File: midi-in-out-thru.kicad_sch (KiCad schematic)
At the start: 20 parts, among them CN1 uC, M1 IN, M2 OUT, M3 THRU, U1 6N138, U1 74HC14, U101 74HC14

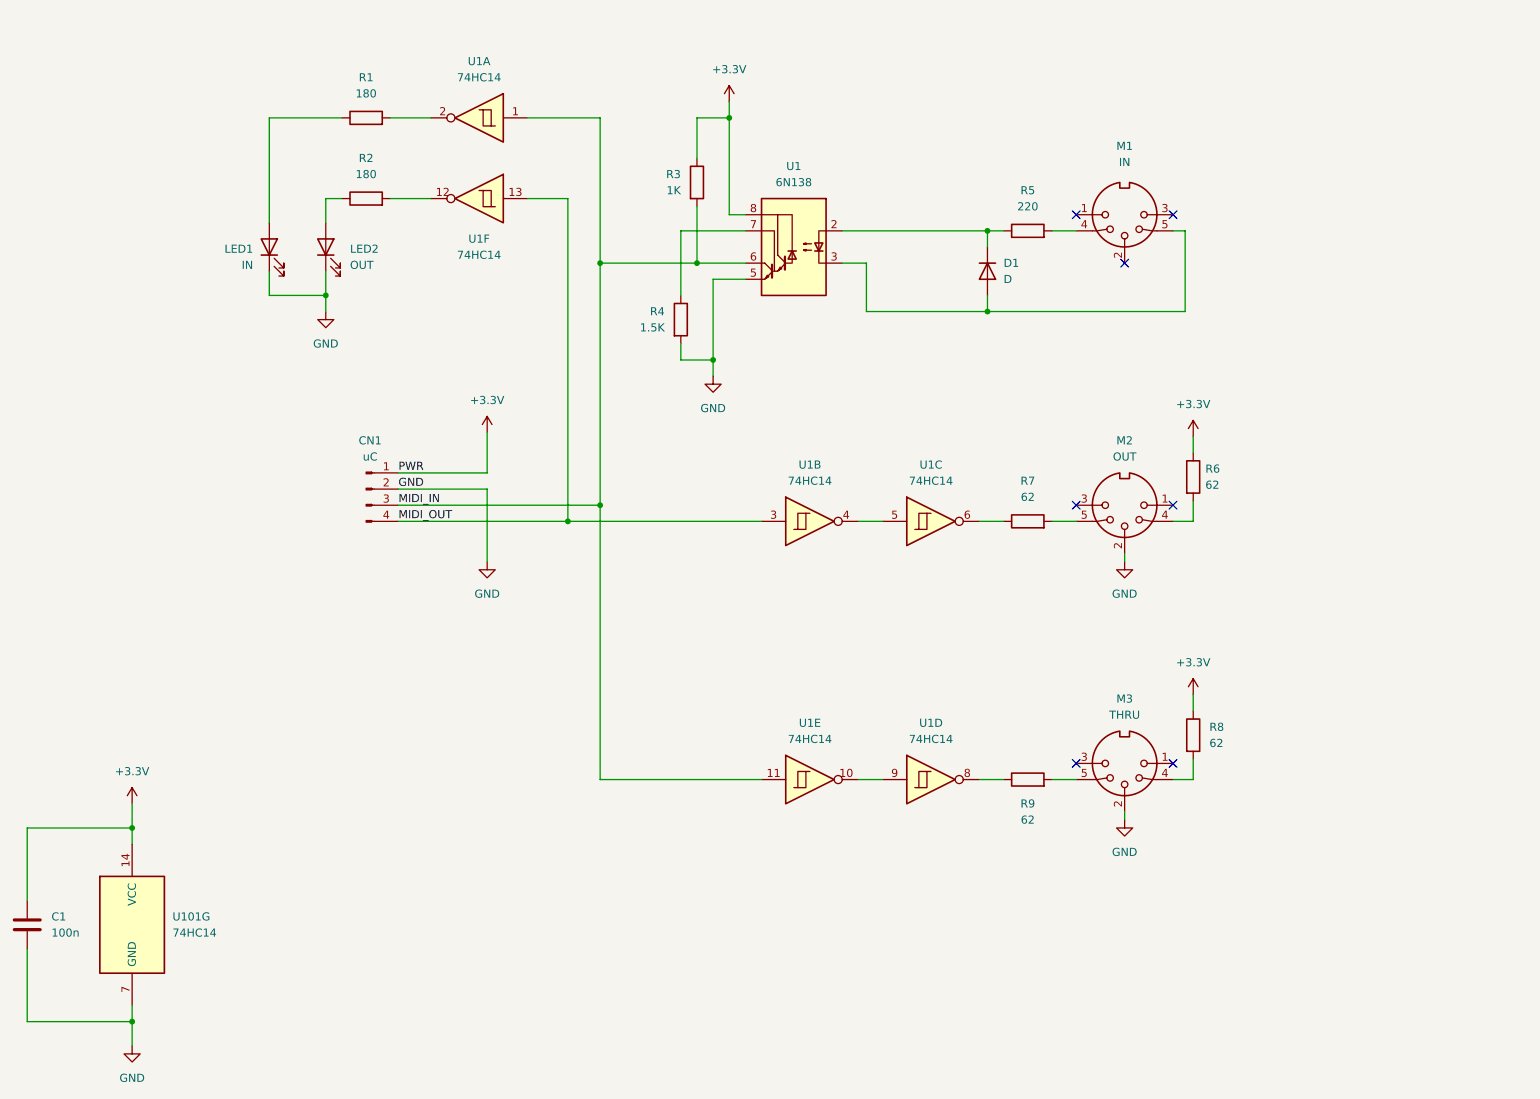
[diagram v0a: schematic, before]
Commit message: Use H11L1
Resistor values taken from CA-033 Update 2014
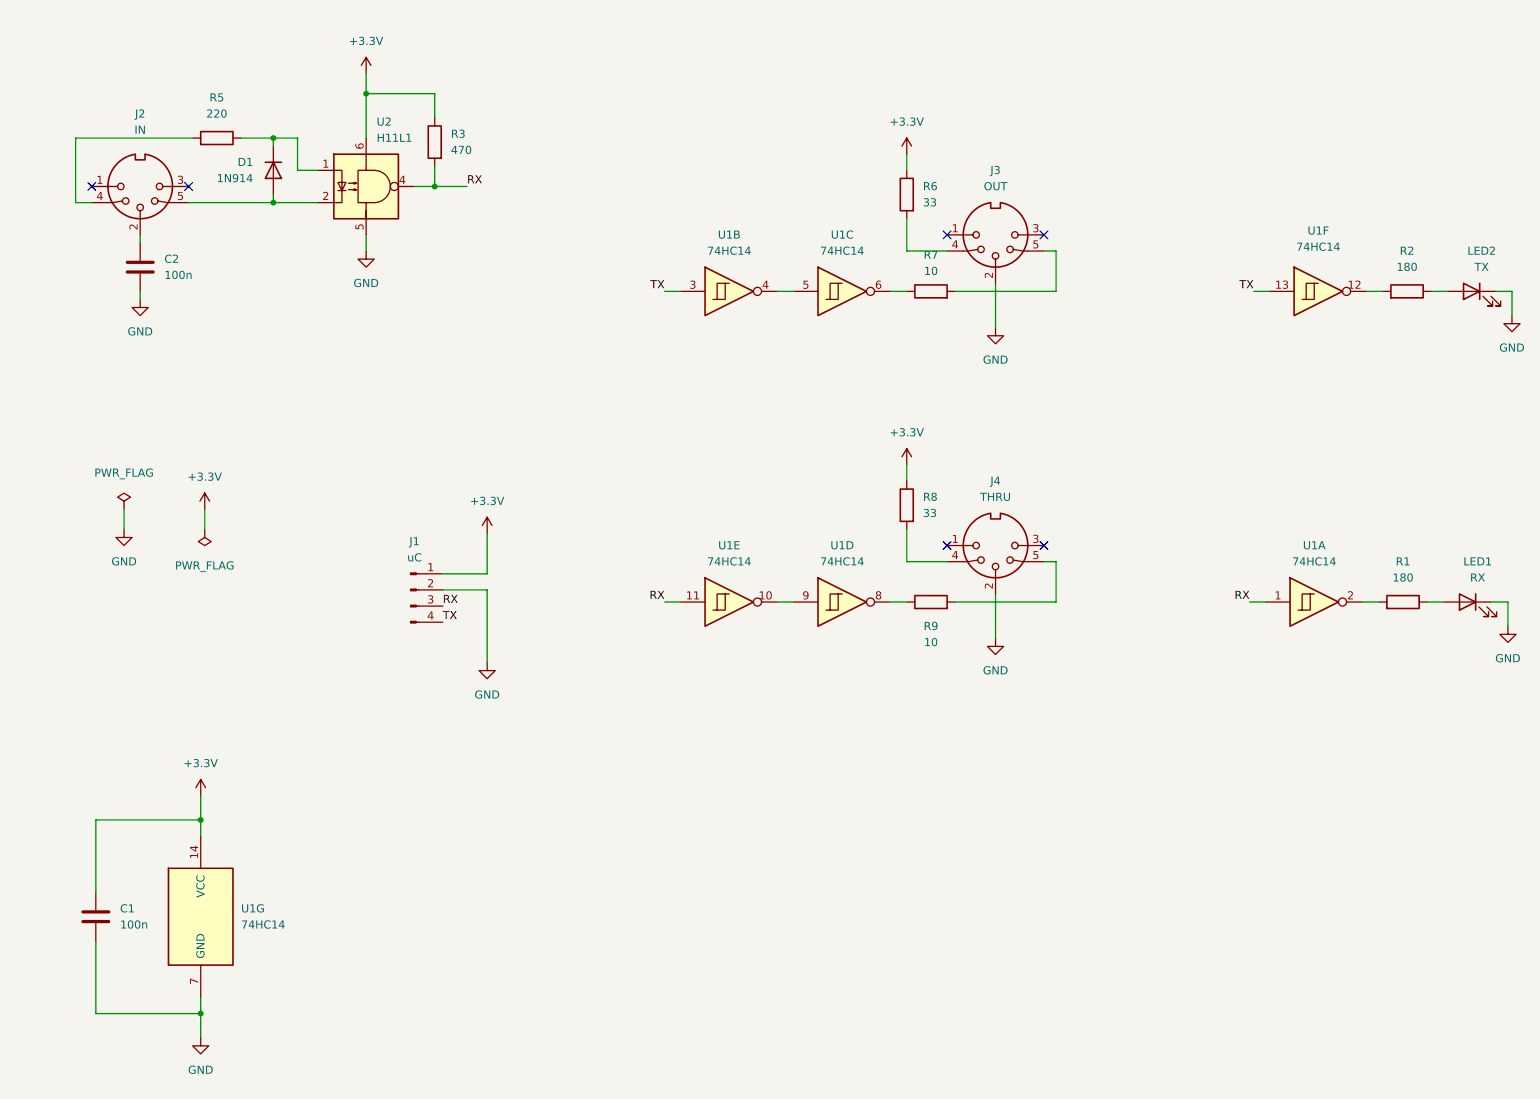
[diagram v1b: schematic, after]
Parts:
- removed D1: D, symbol Device:D
- removed M2: OUT, symbol Connector:DIN-5_180degree
- removed R4: 1.5K, symbol Device:R
- removed U1: 6N138, symbol Isolator:6N138
- added C2: 100n, Capacitor_THT:C_Disc_D3.8mm_W2.6mm_P2.50mm, symbol Device:C
- added D1: 1N914, Diode_THT:D_DO-35_SOD27_P7.62mm_Horizontal, symbol Diode:1N914
- added J3: OUT, symbol Connector:DIN-5_180degree
- added U2: H11L1, Package_DIP:DIP-6_W7.62mm_Socket, symbol Isolator:H11L1
- C1: footprint (none) -> Capacitor_THT:C_Disc_D3.8mm_W2.6mm_P2.50mm
- J1: renamed from CN1; footprint (none) -> Connector_PinHeader_2.54mm:PinHeader_1x04_P2.54mm_Vertical
- LED1: value IN -> RX; footprint (none) -> LED_THT:LED_D3.0mm
- LED2: value OUT -> TX; footprint (none) -> LED_THT:LED_D3.0mm
- R1, R2, R5: footprint (none) -> Resistor_THT:R_Axial_DIN0207_L6.3mm_D2.5mm_P10.16mm_Horizontal
- R3: value 1K -> 470; footprint (none) -> Resistor_THT:R_Axial_DIN0207_L6.3mm_D2.5mm_P10.16mm_Horizontal
- R6, R8: value 62 -> 33; footprint (none) -> Resistor_THT:R_Axial_DIN0207_L6.3mm_D2.5mm_P10.16mm_Horizontal
- R7, R9: value 62 -> 10; footprint (none) -> Resistor_THT:R_Axial_DIN0207_L6.3mm_D2.5mm_P10.16mm_Horizontal
- U1: footprint (none) -> Package_DIP:DIP-14_W7.62mm_Socket
- U1: renamed from U101; footprint (none) -> Package_DIP:DIP-14_W7.62mm_Socket
- renumbered M1 to J2, M3 to J4
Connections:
- net +3.3V: now also U2.6
- net GND: now also C2.2, J3.2, U2.5
- net at R5.1: now also D1.1 (K), U2.1
- net at J2.5: now also D1.2 (A), U2.2
- net at R7.2: now also J3.5
- net at J2.2: now also C2.1
- net at R6.2: now also J3.4
- net MIDI_IN renamed RX
- net RX: now also U2.4
- net MIDI_OUT renamed TX
- no-connect marks 7 -> 6
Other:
- title: (none) -> 3.3V MIDI in/out/thru
- moved on the sheet: C1, J1, J2, J4, LED1, LED2, R1, R2, R5, R8, R9, U1A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

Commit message: Completed initial layout
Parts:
- added C3: 100n, Capacitor_THT:C_Disc_D3.8mm_W2.6mm_P2.50mm, symbol Device:C
- added H1, H2, H3, H4: MountingHole, MountingHole:MountingHole_3.2mm_M3, symbol Mechanical:MountingHole
- J2, J3, J4: footprint (none) -> Personal:MIDI_DIN5
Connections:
- net +3.3V: now also C3.2
- net GND: now also C3.1
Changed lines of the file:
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@@
     (stroke (width 0) (type default) (color 0 0 0 0))
   )
-  (wire (pts (xy 76.2 29.845) (xy 76.2 33.02))
+  (wire (pts (xy 76.2 26.67) (xy 76.2 33.02))
     (stroke (width 0) (type default) (color 0 0 0 0))
   )
@@
     (stroke (width 0) (type default) (color 0 0 0 0))
   )
+  (wire (pts (xy 65.405 33.02) (xy 66.675 33.02))
+    (stroke (width 0) (type default) (color 0 0 0 0))
+  )
   (wire (pts (xy 33.655 147.32) (xy 50.165 147.32))
     (stroke (width 0) (type default) (color 0 0 0 0))
@@
     (stroke (width 0) (type default) (color 0 0 0 0))
   )
+  (wire (pts (xy 74.295 33.02) (xy 76.2 33.02))
+    (stroke (width 0) (type default) (color 0 0 0 0))
+  )
   (wire (pts (xy 68.58 45.085) (xy 65.405 45.085))
     (stroke (width 0) (type default) (color 0 0 0 0))
@@
   )
   (wire (pts (xy 243.205 113.03) (xy 245.745 113.03))
+    (stroke (width 0) (type default) (color 0 0 0 0))
+  )
+  (wire (pts (xy 65.405 34.29) (xy 65.405 33.02))
     (stroke (width 0) (type default) (color 0 0 0 0))
   )
@@
     (effects (font (size 1.27 1.27)) (justify left bottom))
   )
+  (symbol (lib_id "power:GND") (at 65.405 34.29 0) (mirror y) (unit 1)
+    (in_bom yes) (on_board yes) (fields_autoplaced)
+    (property "Reference" "#PWR?" (id 0) (at 65.405 40.64 0)
+      (effects (font (size 1.27 1.27)) hide)
+    )
+    (property "Value" "GND" (id 1) (at 63.5 35.5599 0)
+      (effects (font (size 1.27 1.27)) (justify left))
+    )
+    (property "Footprint" "" (id 2) (at 65.405 34.29 0)
+      (effects (font (size 1.27 1.27)) hide)
+    )
+    (property "Datasheet" "" (id 3) (at 65.405 34.29 0)
+      (effects (font (size 1.27 1.27)) hide)
+    )
+    (pin "1")
+  )
   (symbol (lib_id "power:GND") (at 76.2 57.785 0) (mirror y) (unit 1)
     (in_bom yes) (on_board yes) (fields_autoplaced)
@@
     )
     (pin "1")
+  )
+  (symbol (lib_id "Mechanical:MountingHole") (at 82.55 171.45 0) (unit 1)
+    (in_bom yes) (on_board yes) (fields_autoplaced)
+    (property "Reference" "H3" (id 0) (at 85.09 170.1799 0)
+      (effects (font (size 1.27 1.27)) (justify left))
+    )
+    (property "Value" "MountingHole" (id 1) (at 85.09 172.7199 0)
+      (effects (font (size 1.27 1.27)) (justify left))
+    )
+    (property "Footprint" "MountingHole:MountingHole_3.2mm_M3" (id 2) (at 82.55 171.45 0)
+      (effects (font (size 1.27 1.27)) hide)
+    )
+    (property "Datasheet" "~" (id 3) (at 82.55 171.45 0)
+      (effects (font (size 1.27 1.27)) hide)
+    )
   )
   (symbol (lib_id "Device:R") (at 165.1 64.135 90) (unit 1)
@@
     (property "Reference" "J3" (id 0) (at 175.2601 45.085 0))
     (property "Value" "OUT" (id 1) (at 175.2601 47.625 0))
-    (property "Footprint" "" (id 2) (at 175.26 55.245 0)
+    (property "Footprint" "Personal:MIDI_DIN5" (id 2) (at 175.26 55.245 0)
       (effects (font (size 1.27 1.27)) hide)
     )
@@
     (property "Reference" "J4" (id 0) (at 175.2601 93.98 0))
     (property "Value" "THRU" (id 1) (at 175.2601 96.52 0))
-    (property "Footprint" "" (id 2) (at 175.26 104.14 0)
+    (property "Footprint" "Personal:MIDI_DIN5" (id 2) (at 175.26 104.14 0)
       (effects (font (size 1.27 1.27)) hide)
     )
@@
     (pin "2")
   )
-  (symbol (lib_id "power:+3.3V") (at 76.2 29.845 0) (mirror y) (unit 1)
-    (in_bom yes) (on_board yes) (fields_autoplaced)
-    (property "Reference" "#PWR0103" (id 0) (at 76.2 33.655 0)
-      (effects (font (size 1.27 1.27)) hide)
-    )
-    (property "Value" "+3.3V" (id 1) (at 76.2 24.765 0))
-    (property "Footprint" "" (id 2) (at 76.2 29.845 0)
-      (effects (font (size 1.27 1.27)) hide)
-    )
-    (property "Datasheet" "" (id 3) (at 76.2 29.845 0)
+  (symbol (lib_id "power:+3.3V") (at 76.2 26.67 0) (mirror y) (unit 1)
+    (in_bom yes) (on_board yes) (fields_autoplaced)
+    (property "Reference" "#PWR0103" (id 0) (at 76.2 30.48 0)
+      (effects (font (size 1.27 1.27)) hide)
+    )
+    (property "Value" "+3.3V" (id 1) (at 76.2 21.59 0))
+    (property "Footprint" "" (id 2) (at 76.2 26.67 0)
+      (effects (font (size 1.27 1.27)) hide)
+    )
+    (property "Datasheet" "" (id 3) (at 76.2 26.67 0)
       (effects (font (size 1.27 1.27)) hide)
     )
@@
     (property "Reference" "J2" (id 0) (at 40.6401 36.195 0))
     (property "Value" "IN" (id 1) (at 40.6401 38.735 0))
-    (property "Footprint" "" (id 2) (at 40.64 47.625 0)
+    (property "Footprint" "Personal:MIDI_DIN5" (id 2) (at 40.64 47.625 0)
       (effects (font (size 1.27 1.27)) hide)
     )
@@
     (pin "2")
   )
+  (symbol (lib_id "Mechanical:MountingHole") (at 101.6 171.45 0) (unit 1)
+    (in_bom yes) (on_board yes) (fields_autoplaced)
+    (property "Reference" "H4" (id 0) (at 104.14 170.1799 0)
+      (effects (font (size 1.27 1.27)) (justify left))
+    )
+    (property "Value" "MountingHole" (id 1) (at 104.14 172.7199 0)
+      (effects (font (size 1.27 1.27)) (justify left))
+    )
+    (property "Footprint" "MountingHole:MountingHole_3.2mm_M3" (id 2) (at 101.6 171.45 0)
+      (effects (font (size 1.27 1.27)) hide)
+    )
+    (property "Datasheet" "~" (id 3) (at 101.6 171.45 0)
+      (effects (font (size 1.27 1.27)) hide)
+    )
+  )
   (symbol (lib_id "power:GND") (at 175.26 69.85 0) (mirror y) (unit 1)
     (in_bom yes) (on_board yes) (fields_autoplaced)
@@
     )
     (pin "1")
+  )
+  (symbol (lib_id "Mechanical:MountingHole") (at 101.6 165.1 0) (unit 1)
+    (in_bom yes) (on_board yes) (fields_autoplaced)
+    (property "Reference" "H2" (id 0) (at 104.14 163.8299 0)
+      (effects (font (size 1.27 1.27)) (justify left))
+    )
+    (property "Value" "MountingHole" (id 1) (at 104.14 166.3699 0)
+      (effects (font (size 1.27 1.27)) (justify left))
+    )
+    (property "Footprint" "MountingHole:MountingHole_3.2mm_M3" (id 2) (at 101.6 165.1 0)
+      (effects (font (size 1.27 1.27)) hide)
+    )
+    (property "Datasheet" "~" (id 3) (at 101.6 165.1 0)
+      (effects (font (size 1.27 1.27)) hide)
+    )
   )
   (symbol (lib_id "Connector:Conn_01x04_Male") (at 83.185 111.125 0) (unit 1)
@@
     (pin "1")
   )
+  (symbol (lib_id "Device:C") (at 70.485 33.02 90) (mirror x) (unit 1)
+    (in_bom yes) (on_board yes) (fields_autoplaced)
+    (property "Reference" "C3" (id 0) (at 70.485 25.4 90))
+    (property "Value" "100n" (id 1) (at 70.485 27.94 90))
+    (property "Footprint" "Capacitor_THT:C_Disc_D3.8mm_W2.6mm_P2.50mm" (id 2) (at 74.295 33.9852 0)
+      (effects (font (size 1.27 1.27)) hide)
+    )
+    (property "Datasheet" "~" (id 3) (at 70.485 33.02 0)
+      (effects (font (size 1.27 1.27)) hide)
+    )
+    (pin "1")
+    (pin "2")
+  )
   (symbol (lib_id "74xx:74HC14") (at 225.425 113.03 0) (unit 1)
     (in_bom yes) (on_board yes) (fields_autoplaced)
@@
     (pin "2")
   )
+  (symbol (lib_id "Mechanical:MountingHole") (at 82.55 165.1 0) (unit 1)
+    (in_bom yes) (on_board yes) (fields_autoplaced)
+    (property "Reference" "H1" (id 0) (at 85.09 163.8299 0)
+      (effects (font (size 1.27 1.27)) (justify left))
+    )
+    (property "Value" "MountingHole" (id 1) (at 85.09 166.3699 0)
+      (effects (font (size 1.27 1.27)) (justify left))
+    )
+    (property "Footprint" "MountingHole:MountingHole_3.2mm_M3" (id 2) (at 82.55 165.1 0)
+      (effects (font (size 1.27 1.27)) hide)
+    )
+    (property "Datasheet" "~" (id 3) (at 82.55 165.1 0)
+      (effects (font (size 1.27 1.27)) hide)
+    )
+  )
   (symbol (lib_id "74xx:74HC14") (at 151.13 64.135 0) (unit 3)
     (in_bom yes) (on_board yes) (fields_autoplaced)
@@
       (reference "#PWR0115") (unit 1) (value "+3.3V") (footprint "")
     )
+    (path "/0291a830-67a0-423c-a566-fb34d6d5531f"
+      (reference "#PWR?") (unit 1) (value "GND") (footprint "")
+    )
     (path "/9fea0110-ae43-4274-8d17-1a6e900fe8a4"
       (reference "C1") (unit 1) (value "100n") (footprint "Capacitor_THT:C_Disc_D3.8mm_W2.6mm_P2.50mm")
@@
       (reference "C2") (unit 1) (value "100n") (footprint "Capacitor_THT:C_Disc_D3.8mm_W2.6mm_P2.50mm")
     )
+    (path "/e3fd39bd-aeb0-40c0-b24e-23796547db52"
+      (reference "C3") (unit 1) (value "100n") (footprint "Capacitor_THT:C_Disc_D3.8mm_W2.6mm_P2.50mm")
+    )
     (path "/4a85acf1-118e-42f6-9680-6ff0362bb27b"
       (reference "D1") (unit 1) (value "1N914") (footprint "Diode_THT:D_DO-35_SOD27_P7.62mm_Horizontal")
     )
+    (path "/ee3bc06d-2250-4c1c-b977-ec84578915ae"
+      (reference "H1") (unit 1) (value "MountingHole") (footprint "MountingHole:MountingHole_3.2mm_M3")
+    )
+    (path "/cfa74424-4a16-4630-b6d1-839c02b4b813"
+      (reference "H2") (unit 1) (value "MountingHole") (footprint "MountingHole:MountingHole_3.2mm_M3")
+    )
+    (path "/04e25a40-0d1a-46a4-aca6-6b4084f82503"
+      (reference "H3") (unit 1) (value "MountingHole") (footprint "MountingHole:MountingHole_3.2mm_M3")
+    )
+    (path "/c48e435b-2e86-4bbe-bada-666f3df40f1b"
+      (reference "H4") (unit 1) (value "MountingHole") (footprint "MountingHole:MountingHole_3.2mm_M3")
+    )
     (path "/d69ff862-98f2-4617-95f8-9aaf9c571075"
       (reference "J1") (unit 1) (value "uC") (footprint "Connector_PinHeader_2.54mm:PinHeader_1x04_P2.54mm_Vertical")
     )
     (path "/b0b0b7d6-ddf7-4ca3-8337-449d434b9897"
-      (reference "J2") (unit 1) (value "IN") (footprint "")
+      (reference "J2") (unit 1) (value "IN") (footprint "Personal:MIDI_DIN5")
     )
     (path "/110c4c6e-51b2-4423-ae4d-d191d799bbf0"
-      (reference "J3") (unit 1) (value "OUT") (footprint "")
+      (reference "J3") (unit 1) (value "OUT") (footprint "Personal:MIDI_DIN5")
     )
     (path "/28837119-66a9-4564-86b9-a183314fa7ea"
-      (reference "J4") (unit 1) (value "THRU") (footprint "")
+      (reference "J4") (unit 1) (value "THRU") (footprint "Personal:MIDI_DIN5")
     )
     (path "/b040ec36-dd87-44d0-9a06-70797d228226"
